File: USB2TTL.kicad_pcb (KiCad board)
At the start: 2 copper layers, 30 x 20 mm, 30 parts, among them J1 USB_A, J2 Conn_01x05, Q1 SiA517DJ, SW1 TS-1187A-B-A-B, SW2 TS-1187A-B-A-B, U1 SPX3819M5-L-3-3, U2 CH343P

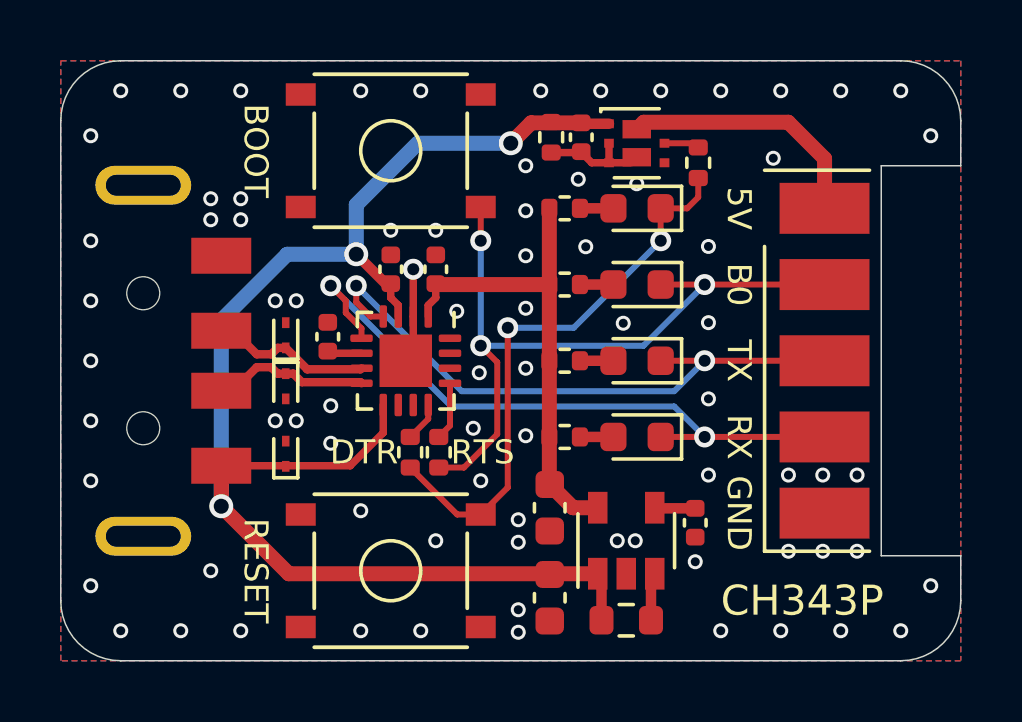
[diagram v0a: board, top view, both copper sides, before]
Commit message: Fix rotation of SiA517DJ
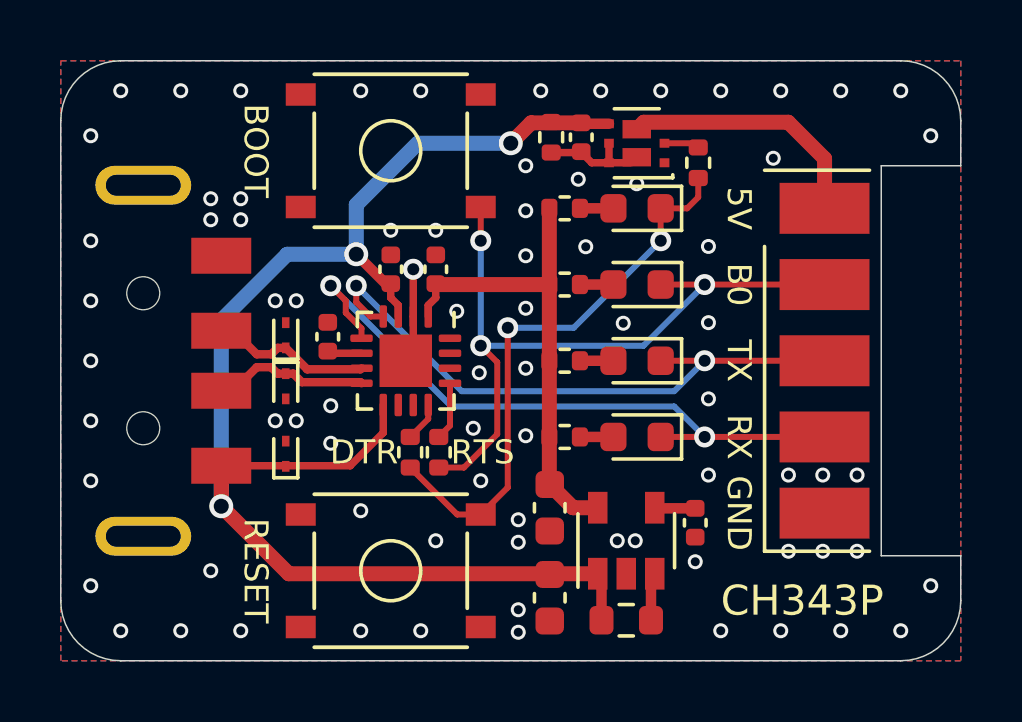
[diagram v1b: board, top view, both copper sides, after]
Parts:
- turned Q1 to 180 degrees
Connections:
- Q1 pad 1: +5V -> GND
- Q1 pad 2: Net-(C4-Pad2) -> Net-(Q1-Pad2)
- Q1 pad 3: Net-(C4-Pad2) -> /VOUT
- Q1 pad 4: GND -> +5V
- Q1 pad 5: Net-(Q1-Pad5) -> Net-(C4-Pad2)
- Q1 pad 6: /VOUT -> Net-(C4-Pad2)
- R3 pad 1: Net-(Q1-Pad5) -> Net-(Q1-Pad2)
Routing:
- net Net-(Q1-Pad5): track 0.98 -> 0.00 mm
- net Net-(Q1-Pad2): track 0.00 -> 0.98 mm
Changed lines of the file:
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@@
   (net 18 /BOOT)
   (net 19 /VOUT)
-  (net 20 "Net-(Q1-Pad5)")
-  (net 21 "Net-(R1-Pad1)")
-  (net 22 /RESET)
+  (net 20 "Net-(R1-Pad1)")
+  (net 21 /RESET)
+  (net 22 "Net-(Q1-Pad2)")
   (net_class Default "This is the default net class."
     (clearance 0.15)
@@
     (add_net "Net-(D7-Pad2)")
     (add_net "Net-(J1-Pad5)")
-    (add_net "Net-(Q1-Pad5)")
+    (add_net "Net-(Q1-Pad2)")
     (add_net "Net-(R1-Pad1)")
   )
@@
       (net 9 /DTR))
     (pad 1 smd roundrect (at -0.51 0 90) (size 0.54 0.64) (layers F.Cu F.Paste F.Mask) (roundrect_rratio 0.25)
-      (net 22 /RESET))
+      (net 21 /RESET))
     (model ${KISYS3DMOD}/Resistor_SMD.3dshapes/R_0402_1005Metric.wrl
       (at (xyz 0 0 0))
@@
     (fp_circle (center 0 0) (end 1 0) (layer F.SilkS) (width 0.12))
     (pad 1 smd rect (at -3 -1.875) (size 1 0.75) (layers F.Cu F.Paste F.Mask)
-      (net 22 /RESET))
+      (net 21 /RESET))
     (pad 1 smd rect (at 3 -1.875) (size 1 0.75) (layers F.Cu F.Paste F.Mask)
-      (net 22 /RESET))
+      (net 21 /RESET))
     (pad 2 smd rect (at -3 1.875) (size 1 0.75) (layers F.Cu F.Paste F.Mask)
       (net 1 GND))
@@
       (net 4 +5V))
     (pad 1 smd roundrect (at -0.825 0 180) (size 0.8 0.95) (layers F.Cu F.Paste F.Mask) (roundrect_rratio 0.25)
-      (net 21 "Net-(R1-Pad1)"))
+      (net 20 "Net-(R1-Pad1)"))
     (model ${KISYS3DMOD}/Resistor_SMD.3dshapes/R_0603_1608Metric.wrl
       (at (xyz 0 0 0))
@@
     )
     (pad 2 smd roundrect (at 0.51 0 270) (size 0.54 0.64) (layers F.Cu F.Paste F.Mask) (roundrect_rratio 0.25)
-      (net 22 /RESET))
+      (net 21 /RESET))
     (pad 1 smd roundrect (at -0.51 0 270) (size 0.54 0.64) (layers F.Cu F.Paste F.Mask) (roundrect_rratio 0.25)
-      (net 20 "Net-(Q1-Pad5)"))
+      (net 22 "Net-(Q1-Pad2)"))
     (model ${KISYS3DMOD}/Resistor_SMD.3dshapes/R_0402_1005Metric.wrl
       (at (xyz 0 0 0))
@@
   )
   (module JLC-SMT:Vishay_PowerPAK_SC70-6L_Dual (layer F.Cu)
-    (at 119.2 102.75)
+    (at 119.2 102.75 180)
     (descr "Vishay PowerPAK SC70 dual transistor package http://www.vishay.com/docs/70487/70487.pdf")
     (tags "powerpak sc70 sc-70 dual")
@@
       (effects (font (size 0.4 0.4) (thickness 0.1)))
     )
-    (pad 6 smd rect (at 0 -0.4665) (size 0.95 0.613) (layers F.Cu F.Paste F.Mask)
+    (pad 6 smd rect (at 0 -0.4665 180) (size 0.95 0.613) (layers F.Cu F.Paste F.Mask)
+      (net 15 "Net-(C4-Pad2)"))
+    (pad 3 smd rect (at 0 0.4665 180) (size 0.95 0.613) (layers F.Cu F.Paste F.Mask)
       (net 19 /VOUT))
-    (pad 3 smd rect (at 0 0.4665) (size 0.95 0.613) (layers F.Cu F.Paste F.Mask)
+    (pad 6 smd rect (at 0.925 -0.65 180) (size 0.325 0.3) (layers F.Cu F.Paste F.Mask)
       (net 15 "Net-(C4-Pad2)"))
-    (pad 6 smd rect (at 0.925 -0.65) (size 0.325 0.3) (layers F.Cu F.Paste F.Mask)
+    (pad 4 smd rect (at 0.925 0.65 180) (size 0.325 0.3) (layers F.Cu F.Paste F.Mask)
+      (net 4 +5V))
+    (pad 5 smd rect (at 0.925 0 180) (size 0.325 0.3) (layers F.Cu F.Paste F.Mask)
+      (net 15 "Net-(C4-Pad2)"))
+    (pad 3 smd rect (at -0.925 0.65 180) (size 0.325 0.3) (layers F.Cu F.Paste F.Mask)
       (net 19 /VOUT))
-    (pad 4 smd rect (at 0.925 0.65) (size 0.325 0.3) (layers F.Cu F.Paste F.Mask)
-      (net 1 GND))
-    (pad 5 smd rect (at 0.925 0) (size 0.325 0.3) (layers F.Cu F.Paste F.Mask)
-      (net 20 "Net-(Q1-Pad5)"))
-    (pad 3 smd rect (at -0.925 0.65) (size 0.325 0.3) (layers F.Cu F.Paste F.Mask)
-      (net 15 "Net-(C4-Pad2)"))
-    (pad 2 smd rect (at -0.925 0) (size 0.325 0.3) (layers F.Cu F.Paste F.Mask)
-      (net 15 "Net-(C4-Pad2)"))
-    (pad 1 smd rect (at -0.925 -0.65) (size 0.325 0.3) (layers F.Cu F.Paste F.Mask)
-      (net 4 +5V))
+    (pad 2 smd rect (at -0.925 0 180) (size 0.325 0.3) (layers F.Cu F.Paste F.Mask)
+      (net 22 "Net-(Q1-Pad2)"))
+    (pad 1 smd rect (at -0.925 -0.65 180) (size 0.325 0.3) (layers F.Cu F.Paste F.Mask)
+      (net 1 GND))
     (model ${KISYS3DMOD}/Package_DFN_QFN.3dshapes/DFN-6-1EP_2x2mm_P0.65mm_EP1x1.6mm.wrl
       (at (xyz 0 0 0))
@@
       (net 17 "Net-(D7-Pad2)"))
     (pad 1 smd roundrect (at -0.7875 0 180) (size 0.875 0.95) (layers F.Cu F.Paste F.Mask) (roundrect_rratio 0.25)
-      (net 22 /RESET))
+      (net 21 /RESET))
     (model ${KISYS3DMOD}/LED_SMD.3dshapes/LED_0603_1608Metric.wrl
       (at (xyz 0 0 0))
@@
       (net 14 "Net-(C2-Pad1)"))
     (pad 3 smd rect (at -1.1 0.95 90) (size 1.06 0.65) (layers F.Cu F.Paste F.Mask)
-      (net 21 "Net-(R1-Pad1)"))
+      (net 20 "Net-(R1-Pad1)"))
     (pad 2 smd rect (at -1.1 0 90) (size 1.06 0.65) (layers F.Cu F.Paste F.Mask)
       (net 1 GND))
@@
   (segment (start 124.25 102.05) (end 119.4335 102.05) (width 0.5) (layer F.Cu) (net 19))
   (segment (start 125.46 103.26) (end 124.25 102.05) (width 0.5) (layer F.Cu) (net 19))
-  (segment (start 120.125 102.75) (end 121.11 102.75) (width 0.2) (layer F.Cu) (net 20))
-  (segment (start 119.675 118.65) (end 119.675 117.225) (width 0.35) (layer F.Cu) (net 21))
-  (segment (start 113.215 115.125) (end 114 115.125) (width 0.2) (layer F.Cu) (net 22))
-  (segment (start 111.65 113.56) (end 113.215 115.125) (width 0.2) (layer F.Cu) (net 22))
-  (segment (start 119.9975 104.92) (end 120.88 104.92) (width 0.2) (layer F.Cu) (net 22))
-  (segment (start 121.25 104.55) (end 121.25 103.91) (width 0.2) (layer F.Cu) (net 22))
-  (segment (start 120.88 104.92) (end 121.25 104.55) (width 0.2) (layer F.Cu) (net 22))
-  (via (at 120 106) (size 0.7) (drill 0.4) (layers F.Cu B.Cu) (net 22))
-  (segment (start 119.9975 105.9975) (end 120 106) (width 0.2) (layer F.Cu) (net 22))
-  (segment (start 119.9975 104.92) (end 119.9975 105.9975) (width 0.2) (layer F.Cu) (net 22))
-  (via (at 114.9 108.9) (size 0.7) (drill 0.4) (layers F.Cu B.Cu) (net 22))
-  (segment (start 120 106) (end 117.1 108.9) (width 0.2) (layer B.Cu) (net 22))
-  (segment (start 114.9 108.9) (end 117.1 108.9) (width 0.2) (layer B.Cu) (net 22))
-  (segment (start 114.9 114.225) (end 114 115.125) (width 0.2) (layer F.Cu) (net 22))
-  (segment (start 114.9 108.9) (end 114.9 114.225) (width 0.2) (layer F.Cu) (net 22))
+  (segment (start 119.675 118.65) (end 119.675 117.225) (width 0.35) (layer F.Cu) (net 20))
+  (segment (start 113.215 115.125) (end 114 115.125) (width 0.2) (layer F.Cu) (net 21))
+  (segment (start 111.65 113.56) (end 113.215 115.125) (width 0.2) (layer F.Cu) (net 21))
+  (segment (start 119.9975 104.92) (end 120.88 104.92) (width 0.2) (layer F.Cu) (net 21))
+  (segment (start 121.25 104.55) (end 121.25 103.91) (width 0.2) (layer F.Cu) (net 21))
+  (segment (start 120.88 104.92) (end 121.25 104.55) (width 0.2) (layer F.Cu) (net 21))
+  (via (at 120 106) (size 0.7) (drill 0.4) (layers F.Cu B.Cu) (net 21))
+  (segment (start 119.9975 105.9975) (end 120 106) (width 0.2) (layer F.Cu) (net 21))
+  (segment (start 119.9975 104.92) (end 119.9975 105.9975) (width 0.2) (layer F.Cu) (net 21))
+  (via (at 114.9 108.9) (size 0.7) (drill 0.4) (layers F.Cu B.Cu) (net 21))
+  (segment (start 120 106) (end 117.1 108.9) (width 0.2) (layer B.Cu) (net 21))
+  (segment (start 114.9 108.9) (end 117.1 108.9) (width 0.2) (layer B.Cu) (net 21))
+  (segment (start 114.9 114.225) (end 114 115.125) (width 0.2) (layer F.Cu) (net 21))
+  (segment (start 114.9 108.9) (end 114.9 114.225) (width 0.2) (layer F.Cu) (net 21))
+  (segment (start 120.125 102.75) (end 121.11 102.75) (width 0.2) (layer F.Cu) (net 22))
   (zone (net 1) (net_name GND) (layer F.Cu) (hatch edge 0.508)
     (connect_pads (clearance 0.15))
